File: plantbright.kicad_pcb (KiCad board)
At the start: 2 copper layers, 34.5 x 48 mm, 21 parts, among them J1 POWER OUT, J2 5V IN, Q1 AO3400A, Q2 AO3400A, Q3 AO3400A, Q5 AO3400A, SW1 USER 0, U1 XIAO-ESP32-C6

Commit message: Enough for tonight, I think the shape works.
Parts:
- R10, R11, R12, R13: moved to F.Cu
- moved Q5 40.5 mm to (140.4, 98.5), turned to -90 degrees
- moved Q3 36.9 mm to (145.9, 98.5), turned to -90 degrees
- moved R8 36.2 mm to (139.3, 94.0), turned to -90 degrees
- moved R13 36.0 mm to (140.4, 103.9)
- moved R7 34.4 mm to (141.4, 94.0), turned to -90 degrees
- moved R6 31.8 mm to (144.8, 94.0), turned to -90 degrees
- moved R5 30.5 mm to (146.9, 94.0), turned to -90 degrees
- moved Q1 29.0 mm to (166.4, 98.3), turned to -90 degrees
- moved R12 28.0 mm to (145.9, 103.9)
- moved Q2 27.8 mm to (160.7, 98.5), turned to -90 degrees
- moved R1 23.9 mm to (167.4, 94.0), turned to -90 degrees
- moved R2 22.8 mm to (165.4, 94.0), turned to -90 degrees
- moved R3 21.6 mm to (161.7, 94.0), turned to -90 degrees
- moved R4 21.5 mm to (159.7, 94.0), turned to -90 degrees
- moved J1 13.3 mm to (153.2, 109.8)
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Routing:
- net +5V: track 42.3 -> 0.00 mm
- net GND: track 2.26 -> 22.2 mm, vias 0 -> 5
- net +3.3V: track 21.8 -> 6.50 mm
- net CH_4: track 0.00 -> 2.20 mm
- net BTN_1: track 9.50 -> 11.6 mm
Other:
- board size 34.5 x 48 mm -> 33 x 54 mm

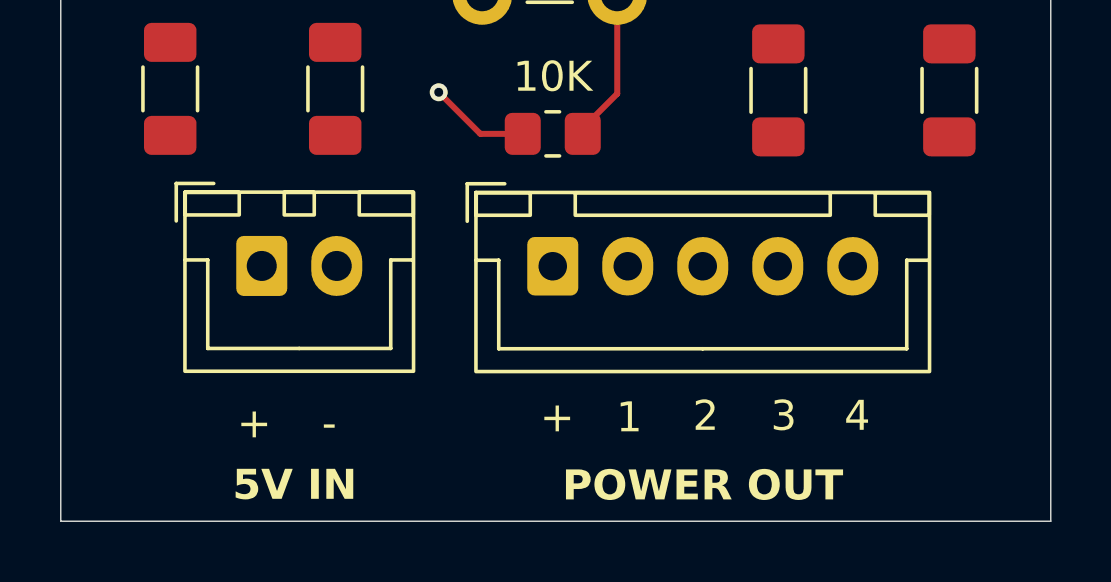
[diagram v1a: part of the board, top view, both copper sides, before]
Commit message: Switch to screw terminals
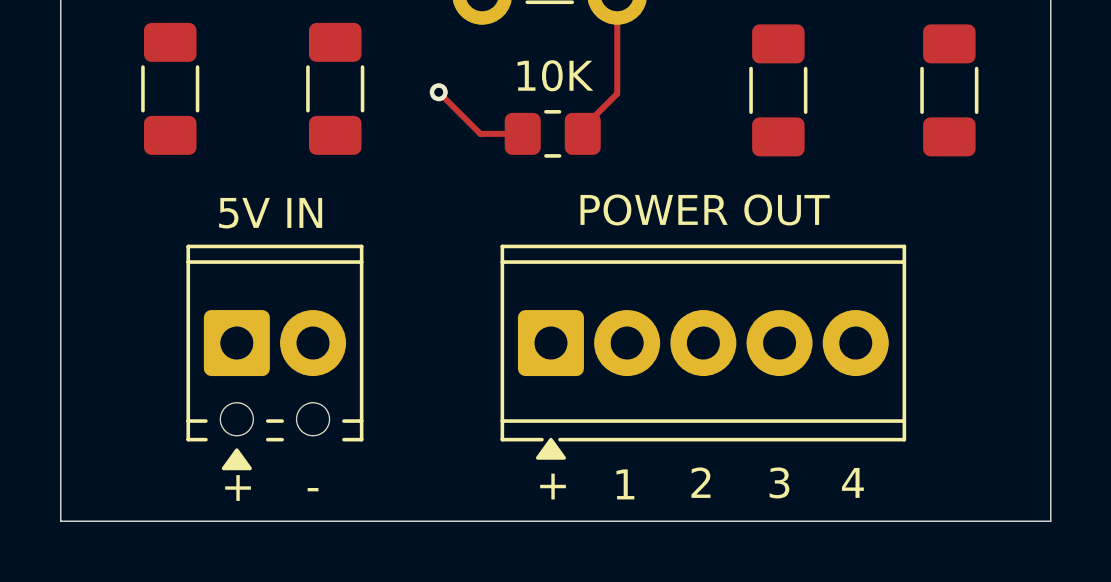
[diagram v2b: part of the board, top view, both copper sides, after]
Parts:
- J1: footprint Connector_JST:JST_XH_B5B-XH-A_1x05_P2.50mm_Vertical -> TerminalBlock_Phoenix:TerminalBlock_Phoenix_MPT-0,5-5-2.54_1x05_P2.54mm_Horizontal
- J2: footprint Connector_JST:JST_XH_B2B-XH-A_1x02_P2.50mm_Vertical -> TerminalBlock_Phoenix:TerminalBlock_Phoenix_MPT-0,5-2-2.54_1x02_P2.54mm_Horizontal
- moved J2 2.70 mm to (142.7, 112.4)
- moved J1 2.56 mm to (153.1, 112.4)

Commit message: Ground pour
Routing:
- net +5V: track 0.00 -> 49.6 mm
- net +3.3V: track 6.50 -> 24.6 mm
- net SW_1: track 0.00 -> 3.16 mm
- net SW_2: track 0.00 -> 2.99 mm
- net SW_3: track 0.00 -> 2.96 mm
- net SW_4: track 0.00 -> 2.89 mm
- net GND: track 22.2 -> 22.8 mm
- added copper zone on B.Cu, net GND
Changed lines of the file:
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@@
+	)
+	(segment
+		(start 166.41 102.42744)
+		(end 166.41 99.27244)
+		(width 0.5)
+		(layer "F.Cu")
+		(net 1)
 	)
 	(segment
@@
 	)
 	(segment
+		(start 137.586223 88.331482)
+		(end 142.577705 83.34)
+		(width 0.5)
+		(layer "F.Cu")
+		(net 3)
+	)
+	(segment
+		(start 142.4 112.4)
+		(end 140.55 110.55)
+		(width 0.5)
+		(layer "F.Cu")
+		(net 3)
+	)
+	(segment
+		(start 142.577705 83.34)
+		(end 145.065 83.34)
+		(width 0.5)
+		(layer "F.Cu")
+		(net 3)
+	)
+	(segment
+		(start 137.541 88.464324)
+		(end 137.586223 88.331482)
+		(width 0.5)
+		(layer "F.Cu")
+		(net 3)
+	)
+	(segment
+		(start 137.541 107.541)
+		(end 137.541 88.464324)
+		(width 0.5)
+		(layer "F.Cu")
+		(net 3)
+	)
+	(segment
+		(start 140.55 110.55)
+		(end 150.55 110.55)
+		(width 0.5)
+		(layer "F.Cu")
+		(net 3)
+	)
+	(segment
+		(start 150.55 110.55)
+		(end 152.4 112.4)
+		(width 0.5)
+		(layer "F.Cu")
+		(net 3)
+	)
+	(segment
+		(start 152.4 112.4)
+		(end 153.13 112.4)
+		(width 0.5)
+		(layer "F.Cu")
+		(net 3)
+	)
+	(segment
+		(start 142.66 112.4)
+		(end 142.66 112.04)
+		(width 0.5)
+		(layer "F.Cu")
+		(net 3)
+	)
+	(segment
+		(start 140.55 110.55)
+		(end 137.541 107.541)
+		(width 0.5)
+		(layer "F.Cu")
+		(net 3)
+	)
+	(segment
+		(start 142.66 112.4)
+		(end 142.4 112.4)
+		(width 0.5)
+		(layer "F.Cu")
+		(net 3)
+	)
+	(segment
+		(start 138.9 100.1)
+		(end 139.49 99.51)
+		(width 0.2)
+		(layer "F.Cu")
+		(net 4)
+	)
+	(segment
 		(start 164.5975 96.43494)
 		(end 163.81 96.43494)
@@
 	)
 	(segment
-		(start 139.49 97.54744)
-		(end 138.5275 96.58494)
-		(width 0.2)
-		(layer "F.Cu")
-		(net 4)
-	)
-	(segment
 		(start 139.49 97.60994)
 		(end 139.49 95.23494)
@@
 	)
 	(segment
+		(start 139.49 99.51)
+		(end 139.49 97.54744)
+		(width 0.2)
+		(layer "F.Cu")
+		(net 4)
+	)
+	(segment
 		(start 144.0275 96.58494)
 		(end 143.24 96.58494)
@@
 	)
 	(segment
-		(start 138.5275 96.58494)
-		(end 137.74 96.58494)
-		(width 0.2)
-		(layer "F.Cu")
-		(net 4)
-	)
-	(segment
 		(start 152.19 105.42744)
 		(end 150.77744 105.42744)
@@
 	)
 	(via
-		(at 137.74 96.58494)
+		(at 138.9 100.1)
 		(size 0.6)
 		(drill 0.3)
@@
 	)
 	(segment
+		(start 160.71 102.42744)
+		(end 160.71 99.44)
+		(width 0.5)
+		(layer "F.Cu")
+		(net 6)
+	)
+	(segment
 		(start 146.94 94.98494)
 		(end 146.94 97.43494)
@@
 	)
 	(segment
+		(start 145.94 102.37744)
+		(end 145.94 99.42244)
+		(width 0.5)
+		(layer "F.Cu")
+		(net 8)
+	)
+	(segment
+		(start 140.44 102.37744)
+		(end 140.44 99.48494)
+		(width 0.5)
+		(layer "F.Cu")
+		(net 9)
+	)
+	(segment
 		(start 141.34 94.98494)
 		(end 141.34 97.55994)
@@
 		(net 17)
 	)
+	(segment
+		(start 150.84 83.2)
+		(end 145.9 78.26)
+		(width 0.2)
+		(layer "B.Cu")
+		(net 17)
+	)
+	(segment
+		(start 150.84 94.29)
+		(end 150.84 83.2)
+		(width 0.2)
+		(layer "B.Cu")
+		(net 17)
+	)
+	(zone
+		(net 4)
+		(net_name "GND")
+		(layer "B.Cu")
+		(hatch edge 0.5)
+		(connect_pads
+			(clearance 0.5)
+		)
+		(min_thickness 0.25)
+		(filled_areas_thickness no)
+		(fill
+			(thermal_gap 0.5)
+			(thermal_bridge_width 0.5)
+		)
+		(polygon
+			(pts
+				(xy 141.5 66.7) (xy 141.5 77) (xy 137.5 88.5) (xy 137.5 117.5) (xy 169 117.5) (xy 169 88.5) (xy 165.5 76.5)
+				(xy 165.5 66.5)
+			)
+		)
+	)
 	(embedded_fonts no)

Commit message: Update plantbright.kicad_pcb
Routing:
- net GND: track 22.8 -> 23.5 mm
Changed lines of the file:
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@@
-	)
-	(segment
-		(start 164.5975 96.43494)
-		(end 163.81 96.43494)
-		(width 0.2)
-		(layer "F.Cu")
-		(net 4)
 	)
 	(segment
@@
 	)
 	(segment
-		(start 165.56 97.39744)
-		(end 164.5975 96.43494)
-		(width 0.2)
-		(layer "F.Cu")
-		(net 4)
-	)
-	(segment
 		(start 144.99 95.13494)
 		(end 144.84 94.98494)
@@
 	)
 	(segment
+		(start 165.56 99.44)
+		(end 165.56 97.39744)
+		(width 0.2)
+		(layer "F.Cu")
+		(net 4)
+	)
+	(segment
 		(start 158.7975 96.63494)
 		(end 158.01 96.63494)
+		(width 0.2)
+		(layer "F.Cu")
+		(net 4)
+	)
+	(segment
+		(start 165 100)
+		(end 165.56 99.44)
 		(width 0.2)
 		(layer "F.Cu")
@@
 	)
 	(via
-		(at 163.81 96.43494)
+		(at 165 100)
 		(size 0.6)
 		(drill 0.3)
